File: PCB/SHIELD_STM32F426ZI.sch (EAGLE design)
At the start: 13 parts, among them IC1 AS4C16M16SA-6TCN, J1 104239-1430

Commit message: neuste vision
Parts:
- added R1, R2: 4.7k, sicom_universal:R_0402WEB_0402
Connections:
- removed net N$103: STM32F4G$5.PE1
- removed net N$111: STM32F4G$5.PG11
- removed net N$160: STM32F4G$6.PE0
- removed net N$23: STM32F4G$5.PC10
- removed net N$25: STM32F4G$5.PC12
- removed net N$54: STM32F4G$5.PD2
- new net N$1: STM32F4G$6.PB8
- net 3.3V: now also R1.2, R2.2
- net DCMI_D2: now also STM32F4G$6.PE0; no longer STM32F4G$6.PC8
- net DCMI_D3: now also STM32F4G$5.PE1; no longer STM32F4G$6.PC9
- net I2C1_SCL: now also R2.1
- net I2C1_SDA: now also R1.1
- net SDIO_CK: now also STM32F4G$5.PC12
- net SDIO_CMD: now also STM32F4G$5.PD2
- net SDIO_D0: now also STM32F4G$6.PC8
- net SDIO_D1: now also STM32F4G$6.PC9
- net SDIO_D2: now also STM32F4G$5.PC10
- net SDIO_D3: now also STM32F4G$5.PC11
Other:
- note added: "I2C"
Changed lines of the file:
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@@
 <part name="R30" library="rcl" library_urn="urn:adsk.eagle:library:334" deviceset="R-EU_" device="R0402" package3d_urn="urn:adsk.eagle:package:23547/3" value="100k"/>
 <part name="R31" library="rcl" library_urn="urn:adsk.eagle:library:334" deviceset="R-EU_" device="R0402" package3d_urn="urn:adsk.eagle:package:23547/3" value="100k"/>
+<part name="R1" library="sicom_universal" library_urn="urn:adsk.eagle:library:5101580" deviceset="R_0402" device="WEB_0402" package3d_urn="urn:adsk.eagle:package:23679/2" value="4.7k"/>
+<part name="R2" library="sicom_universal" library_urn="urn:adsk.eagle:library:5101580" deviceset="R_0402" device="WEB_0402" package3d_urn="urn:adsk.eagle:package:23679/2" value="4.7k"/>
 </parts>
 <sheets>
@@
 <pinref part="STM32F4" gate="G$5" pin="PG15"/>
 <wire x1="236.22" y1="66.04" x2="223.52" y2="66.04" width="0.1524" layer="91"/>
-<label x="213.36" y="66.04" size="1.778" layer="95"/>
+<label x="210.82" y="66.04" size="1.778" layer="95"/>
 </segment>
 </net>
@@
 <pinref part="STM32F4" gate="G$6" pin="PF11"/>
 <wire x1="43.18" y1="60.96" x2="30.48" y2="60.96" width="0.1524" layer="91"/>
-<label x="22.86" y="60.96" size="1.778" layer="95"/>
+<label x="20.32" y="60.96" size="1.778" layer="95"/>
 </segment>
 </net>
@@
 <pinref part="STM32F4" gate="G$6" pin="PG8"/>
 <wire x1="43.18" y1="55.88" x2="30.48" y2="55.88" width="0.1524" layer="91"/>
-<label x="22.86" y="55.88" size="1.778" layer="95"/>
+<label x="20.32" y="55.88" size="1.778" layer="95"/>
 </segment>
 </net>
@@
 </segment>
 </net>
-<net name="N$23" class="0">
+<net name="SDIO_D2" class="0">
 <segment>
 <pinref part="STM32F4" gate="G$5" pin="PC10"/>
 <wire x1="266.7" y1="144.78" x2="279.4" y2="144.78" width="0.1524" layer="91"/>
-</segment>
-</net>
-<net name="N$25" class="0">
+<label x="271.78" y="144.78" size="1.778" layer="95"/>
+</segment>
+</net>
+<net name="SDIO_CK" class="0">
 <segment>
 <pinref part="STM32F4" gate="G$5" pin="PC12"/>
 <wire x1="266.7" y1="142.24" x2="279.4" y2="142.24" width="0.1524" layer="91"/>
-</segment>
-</net>
-<net name="N$54" class="0">
+<label x="271.78" y="142.24" size="1.778" layer="95"/>
+</segment>
+</net>
+<net name="SDIO_CMD" class="0">
 <segment>
 <pinref part="STM32F4" gate="G$5" pin="PD2"/>
 <wire x1="236.22" y1="142.24" x2="223.52" y2="142.24" width="0.1524" layer="91"/>
+<label x="218.44" y="142.24" size="1.778" layer="95"/>
 </segment>
 </net>
@@
 </segment>
 </net>
-<net name="N$103" class="0">
-<segment>
-<pinref part="STM32F4" gate="G$5" pin="PE1"/>
-<wire x1="266.7" y1="68.58" x2="279.4" y2="68.58" width="0.1524" layer="91"/>
-</segment>
-</net>
 <net name="N$107" class="0">
 <segment>
@@
 </segment>
 </net>
-<net name="N$108" class="0">
-<segment>
-<pinref part="STM32F4" gate="G$5" pin="PG10"/>
-<wire x1="236.22" y1="63.5" x2="223.52" y2="63.5" width="0.1524" layer="91"/>
-</segment>
-</net>
 <net name="N$109" class="0">
 <segment>
@@
 </segment>
 </net>
-<net name="N$111" class="0">
-<segment>
-<pinref part="STM32F4" gate="G$5" pin="PG11"/>
-<wire x1="236.22" y1="58.42" x2="223.52" y2="58.42" width="0.1524" layer="91"/>
-</segment>
-</net>
 <net name="N$48" class="0">
 <segment>
@@
 <pinref part="STM32F4" gate="G$6" pin="PG14"/>
 <wire x1="73.66" y1="60.96" x2="86.36" y2="60.96" width="0.1524" layer="91"/>
-</segment>
-</net>
-<net name="N$160" class="0">
-<segment>
-<pinref part="STM32F4" gate="G$6" pin="PE0"/>
-<wire x1="43.18" y1="58.42" x2="30.48" y2="58.42" width="0.1524" layer="91"/>
 </segment>
 </net>
@@
 <pinref part="STM32F4" gate="G$5" pin="PE5"/>
 <wire x1="236.22" y1="83.82" x2="223.52" y2="83.82" width="0.1524" layer="91"/>
-<label x="218.44" y="83.82" size="1.9304" layer="95"/>
+<label x="215.9" y="83.82" size="1.9304" layer="95"/>
 </segment>
 </net>
@@
 </segment>
 <segment>
-<pinref part="STM32F4" gate="G$6" pin="PC9"/>
-<wire x1="73.66" y1="137.16" x2="86.36" y2="137.16" width="0.1524" layer="91"/>
-<label x="81.28" y="137.16" size="1.9304" layer="95"/>
+<pinref part="STM32F4" gate="G$5" pin="PE1"/>
+<wire x1="266.7" y1="68.58" x2="279.4" y2="68.58" width="0.1524" layer="91"/>
+<label x="274.32" y="68.58" size="1.778" layer="95"/>
 </segment>
 </net>
@@
 </segment>
 <segment>
-<pinref part="STM32F4" gate="G$6" pin="PC8"/>
-<wire x1="43.18" y1="137.16" x2="30.48" y2="137.16" width="0.1524" layer="91"/>
-<label x="25.4" y="137.16" size="1.9304" layer="95"/>
+<pinref part="STM32F4" gate="G$6" pin="PE0"/>
+<wire x1="43.18" y1="58.42" x2="30.48" y2="58.42" width="0.1524" layer="91"/>
+<label x="25.4" y="58.42" size="1.778" layer="95"/>
 </segment>
 </net>
@@
 <wire x1="-15.24" y1="15.24" x2="0" y2="15.24" width="0.1524" layer="91"/>
 <label x="-7.62" y="15.24" size="1.9304" layer="95"/>
+</segment>
+</net>
+<net name="N$1" class="0">
+<segment>
+<pinref part="STM32F4" gate="G$6" pin="PB8"/>
+<wire x1="73.66" y1="134.62" x2="86.36" y2="134.62" width="0.1524" layer="91"/>
+</segment>
+</net>
+<net name="SDIO_D1" class="0">
+<segment>
+<pinref part="STM32F4" gate="G$6" pin="PC9"/>
+<wire x1="73.66" y1="137.16" x2="86.36" y2="137.16" width="0.1524" layer="91"/>
+<label x="78.74" y="137.16" size="1.778" layer="95"/>
+</segment>
+</net>
+<net name="SDIO_D0" class="0">
+<segment>
+<pinref part="STM32F4" gate="G$6" pin="PC8"/>
+<wire x1="43.18" y1="137.16" x2="30.48" y2="137.16" width="0.1524" layer="91"/>
+<label x="27.94" y="137.16" size="1.778" layer="95"/>
+</segment>
+</net>
+<net name="SDIO_D3" class="0">
+<segment>
+<pinref part="STM32F4" gate="G$5" pin="PC11"/>
+<wire x1="236.22" y1="144.78" x2="223.52" y2="144.78" width="0.1524" layer="91"/>
+<label x="220.98" y="144.78" size="1.778" layer="95"/>
+</segment>
+</net>
+<net name="N$2" class="0">
+<segment>
+<pinref part="STM32F4" gate="G$5" pin="PG10"/>
+<wire x1="236.22" y1="63.5" x2="223.52" y2="63.5" width="0.1524" layer="91"/>
 </segment>
 </net>
@@
 <plain>
 <text x="66.04" y="88.9" size="3.81" layer="91">SDCARD_MODUL</text>
+<text x="205.232" y="95.758" size="3.81" layer="90">I2C</text>
 </plain>
 <instances>
@@
 <attribute name="NAME" x="138.6586" y="107.95" size="1.778" layer="95" rot="R270"/>
 <attribute name="VALUE" x="133.858" y="107.95" size="1.778" layer="96" rot="R270"/>
+</instance>
+<instance part="R1" gate="G$1" x="223.012" y="72.898" smashed="yes" rot="R90">
+<attribute name="NAME" x="221.5134" y="69.088" size="1.778" layer="95" rot="R90"/>
+<attribute name="VALUE" x="226.314" y="69.088" size="1.778" layer="96" rot="R90"/>
+</instance>
+<instance part="R2" gate="G$1" x="230.632" y="72.898" smashed="yes" rot="R90">
+<attribute name="NAME" x="229.1334" y="69.088" size="1.778" layer="95" rot="R90"/>
+<attribute name="VALUE" x="233.934" y="69.088" size="1.778" layer="96" rot="R90"/>
 </instance>
 </instances>
@@
 <label x="132.08" y="132.08" size="1.778" layer="95"/>
 </segment>
-</net>
+<segment>
+<wire x1="223.012" y1="77.978" x2="223.012" y2="83.058" width="0.1524" layer="91"/>
+<wire x1="223.012" y1="83.058" x2="223.012" y2="93.218" width="0.1524" layer="91"/>
+<wire x1="230.632" y1="77.978" x2="230.632" y2="83.058" width="0.1524" layer="91"/>
+<wire x1="230.632" y1="83.058" x2="223.012" y2="83.058" width="0.1524" layer="91"/>
+<junction x="223.012" y="83.058"/>
+<wire x1="223.012" y1="93.218" x2="210.312" y2="93.218" width="0.1524" layer="91"/>
+<pinref part="R1" gate="G$1" pin="2"/>
+<pinref part="R2" gate="G$1" pin="2"/>
+<label x="212.852" y="93.218" size="1.778" layer="95"/>
+</segment>
+</net>
+<net name="I2C1_SDA" class="0">
+<segment>
+<wire x1="210.312" y1="60.198" x2="223.012" y2="60.198" width="0.1524" layer="91"/>
+<wire x1="223.012" y1="60.198" x2="245.872" y2="60.198" width="0.1524" layer="91"/>
+<wire x1="223.012" y1="60.198" x2="223.012" y2="67.818" width="0.1524" layer="91"/>
+<junction x="223.012" y="60.198"/>
+<pinref part="R1" gate="G$1" pin="1"/>
+<label x="207.772" y="60.198" size="1.778" layer="95"/>
+</segment>
+</net>
+<net name="I2C1_SCL" class="0">
+<segment>
+<wire x1="210.312" y1="57.658" x2="230.632" y2="57.658" width="0.1524" layer="91"/>
+<wire x1="230.632" y1="57.658" x2="245.872" y2="57.658" width="0.1524" layer="91"/>
+<wire x1="230.632" y1="57.658" x2="230.632" y2="67.818" width="0.1524" layer="91"/>
+<pinref part="R2" gate="G$1" pin="1"/>
+<label x="207.772" y="57.658" size="1.778" layer="95"/>
+<junction x="230.632" y="57.658"/>
+</segment>
+</net>

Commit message: neuster Stand
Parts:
- added R3: 10k, sicom_universal:R_0402WEB_0402
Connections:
- net N$1 renamed A
- removed net N$19: IC1.CS#
- net 3.3V: now also R3.2
- net FMC_SDNE0: now also IC1.CS#, R3.1
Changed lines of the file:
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@@
 <part name="R1" library="sicom_universal" library_urn="urn:adsk.eagle:library:5101580" deviceset="R_0402" device="WEB_0402" package3d_urn="urn:adsk.eagle:package:23679/2" value="4.7k"/>
 <part name="R2" library="sicom_universal" library_urn="urn:adsk.eagle:library:5101580" deviceset="R_0402" device="WEB_0402" package3d_urn="urn:adsk.eagle:package:23679/2" value="4.7k"/>
+<part name="R3" library="sicom_universal" library_urn="urn:adsk.eagle:library:5101580" deviceset="R_0402" device="WEB_0402" package3d_urn="urn:adsk.eagle:package:23679/2" value="10k"/>
 </parts>
 <sheets>
@@
 <attribute name="VALUE" x="-85.725" y="98.425" size="1.778" layer="96"/>
 </instance>
+<instance part="R3" gate="G$1" x="-63.5" y="83.82" smashed="yes" rot="R90">
+<attribute name="NAME" x="-64.9986" y="80.01" size="1.778" layer="95" rot="R90"/>
+<attribute name="VALUE" x="-60.198" y="80.01" size="1.778" layer="96" rot="R90"/>
+</instance>
 </instances>
 <busses>
@@
 <wire x1="43.18" y1="60.96" x2="30.48" y2="60.96" width="0.1524" layer="91"/>
 <label x="20.32" y="60.96" size="1.778" layer="95"/>
-</segment>
-</net>
-<net name="N$19" class="0">
-<segment>
-<pinref part="IC1" gate="G$1" pin="CS#"/>
-<wire x1="-33.02" y1="76.2" x2="-45.72" y2="76.2" width="0.1524" layer="91"/>
 </segment>
 </net>
@@
 <label x="-43.18" y="55.88" size="1.9304" layer="95"/>
 </segment>
+<segment>
+<pinref part="R3" gate="G$1" pin="2"/>
+<wire x1="-63.5" y1="88.9" x2="-63.5" y2="93.98" width="0.1524" layer="91"/>
+<label x="-63.5" y="93.98" size="1.778" layer="95"/>
+</segment>
 </net>
 <net name="N$65" class="0">
@@
 <label x="274.32" y="101.6" size="1.778" layer="95"/>
 </segment>
+<segment>
+<pinref part="IC1" gate="G$1" pin="CS#"/>
+<pinref part="R3" gate="G$1" pin="1"/>
+<wire x1="-63.5" y1="78.74" x2="-63.5" y2="76.2" width="0.1524" layer="91"/>
+<wire x1="-63.5" y1="76.2" x2="-33.02" y2="76.2" width="0.1524" layer="91"/>
+<wire x1="-78.74" y1="76.2" x2="-63.5" y2="76.2" width="0.1524" layer="91"/>
+<junction x="-63.5" y="76.2"/>
+<label x="-78.74" y="76.2" size="1.778" layer="95"/>
+</segment>
 </net>
 <net name="N$81" class="0">
@@
 </segment>
 </net>
-<net name="N$1" class="0">
-<segment>
-<pinref part="STM32F4" gate="G$6" pin="PB8"/>
-<wire x1="73.66" y1="134.62" x2="86.36" y2="134.62" width="0.1524" layer="91"/>
-</segment>
-</net>
 <net name="SDIO_D1" class="0">
 <segment>
@@
 </segment>
 </net>
+<net name="A" class="0">
+<segment>
+<pinref part="STM32F4" gate="G$6" pin="PB8"/>
+<wire x1="73.66" y1="134.62" x2="86.36" y2="134.62" width="0.1524" layer="91"/>
+</segment>
+</net>

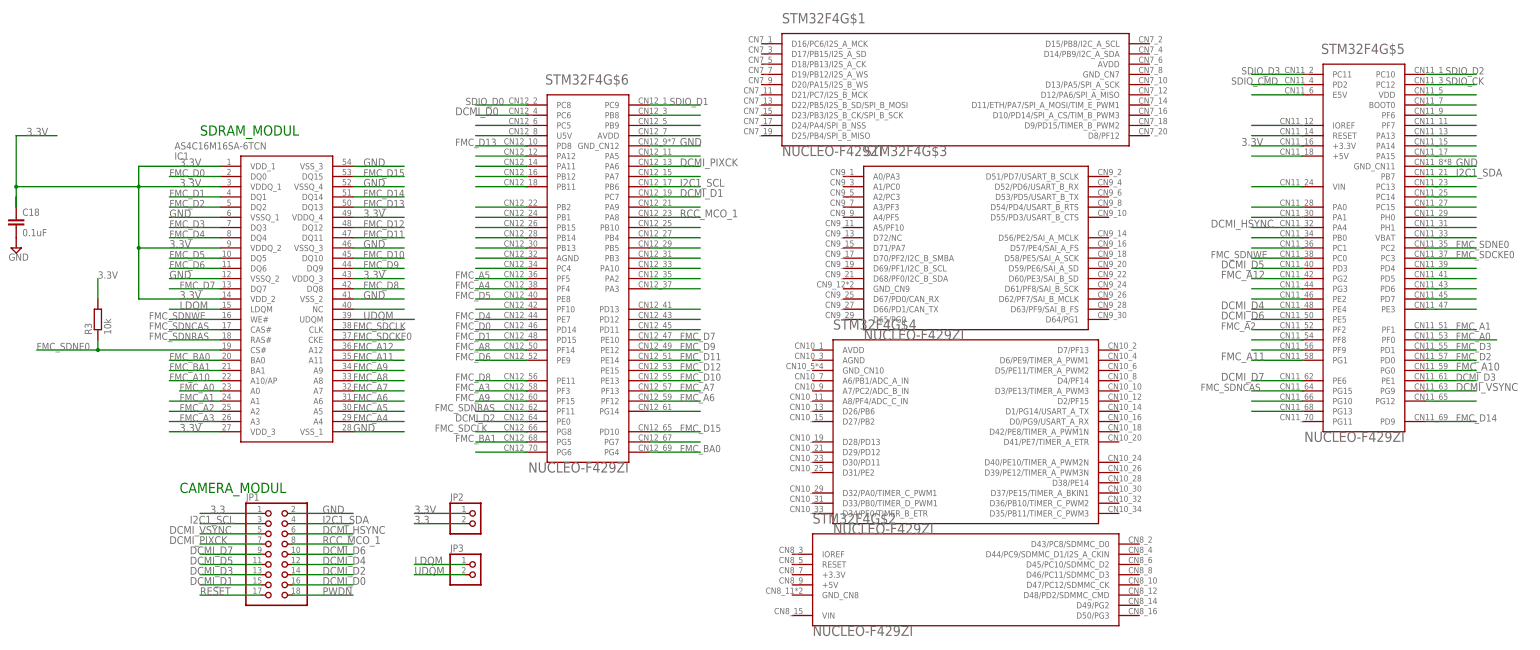
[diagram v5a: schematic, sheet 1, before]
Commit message: modyfi fault by ERC and DRC
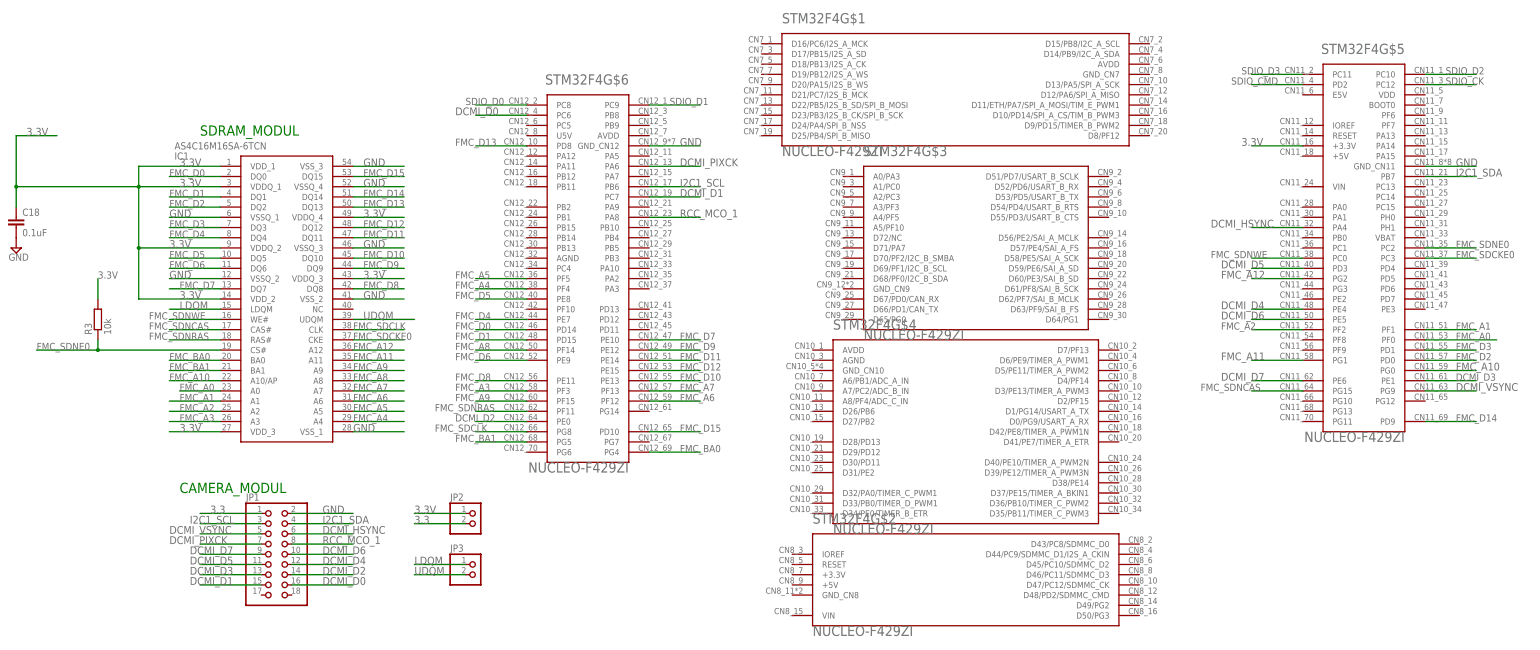
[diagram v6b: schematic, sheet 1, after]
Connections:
- removed net 3V3: J1.T4_VDD
- removed net A: STM32F4G$6.PB8
- removed net N$107: STM32F4G$5.PG12
- removed net N$109: STM32F4G$5.PG13
- removed net N$112: STM32F4G$6.PA12
- removed net N$114: STM32F4G$6.PA11
- removed net N$115: STM32F4G$6.PA7
- removed net N$116: STM32F4G$6.PB12
- removed net N$118: STM32F4G$6.PB11
- removed net N$120: STM32F4G$6.PA9
- removed net N$121: STM32F4G$6.PB2
- removed net N$123: STM32F4G$6.PB1
- removed net N$124: STM32F4G$6.PB10
- removed net N$125: STM32F4G$6.PB15
- removed net N$126: STM32F4G$6.PB4
- removed net N$127: STM32F4G$6.PB14
- removed net N$128: STM32F4G$6.PB5
- removed net N$129: STM32F4G$6.PB13
- removed net N$130: STM32F4G$6.PB3
- removed net N$131: STM32F4G$6.AGND
- removed net N$132: STM32F4G$6.PA10
- removed net N$133: STM32F4G$6.PC4
- removed net N$134: STM32F4G$6.PA2
- removed net N$136: STM32F4G$6.PA3
- removed net N$139: STM32F4G$6.PD13
- removed net N$140: STM32F4G$6.PF10
- removed net N$141: STM32F4G$6.PD12
- removed net N$143: STM32F4G$6.PD11
- removed net N$158: STM32F4G$6.PG14
- removed net N$163: STM32F4G$6.PG7
- removed net N$166: STM32F4G$6.PG6
- removed net N$2: STM32F4G$5.PG10
- removed net N$41: IC1.NC
- removed net N$48: STM32F4G$6.PB9
- removed net N$49: STM32F4G$6.PC5
- removed net N$50: STM32F4G$6.AVDD
- removed net N$51: STM32F4G$6.U5V
- removed net N$55: STM32F4G$5.VDD
- removed net N$56: STM32F4G$5.E5V
- removed net N$57: STM32F4G$5.BOOT0
- removed net N$58: STM32F4G$5.PF6
- removed net N$59: STM32F4G$5.PF7
- removed net N$60: STM32F4G$5.IOREF
- removed net N$61: STM32F4G$5.PA13
- removed net N$62: STM32F4G$5.RESET
- removed net N$63: STM32F4G$5.PA14
- removed net N$65: STM32F4G$5.PA15
- removed net N$66: STM32F4G$5.+5V
- removed net N$69: STM32F4G$5.PC13
- removed net N$70: STM32F4G$5.VIN
- removed net N$71: STM32F4G$5.PC14
- removed net N$72: STM32F4G$5.PC15
- removed net N$73: STM32F4G$5.PA0
- removed net N$74: STM32F4G$5.PH0
- removed net N$75: STM32F4G$5.PA1
- removed net N$76: STM32F4G$5.PH1
- removed net N$78: STM32F4G$5.VBAT
- removed net N$79: STM32F4G$5.PB0
- removed net N$81: STM32F4G$5.PC1
- removed net N$84: STM32F4G$5.PD4
- removed net N$86: STM32F4G$5.PD5
- removed net N$88: STM32F4G$5.PD6
- removed net N$89: STM32F4G$5.PG3
- removed net N$90: STM32F4G$5.PD7
- removed net N$91: STM32F4G$5.PE2
- removed net N$92: STM32F4G$5.PE3
- removed net N$96: STM32F4G$6.PA5
- removed net N$97: STM32F4G$5.PF8
- removed net N$99: STM32F4G$5.PF9
- removed net PWDN: JP1.18
- removed net RESET: JP1.17
- net 3.3V: now also J1.T4_VDD

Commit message: PCB wurde mit kurzer Leitung korrigiert
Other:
- moved on the sheet: C18, IC1, R3, STM32F4G$5, STM32F4G$6

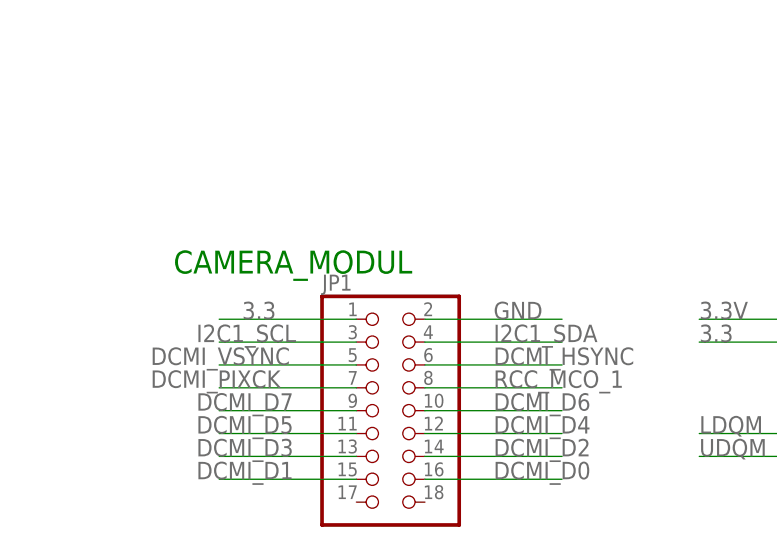
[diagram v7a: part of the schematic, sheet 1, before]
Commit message: Namen der Elementen und Pin hinzufügen
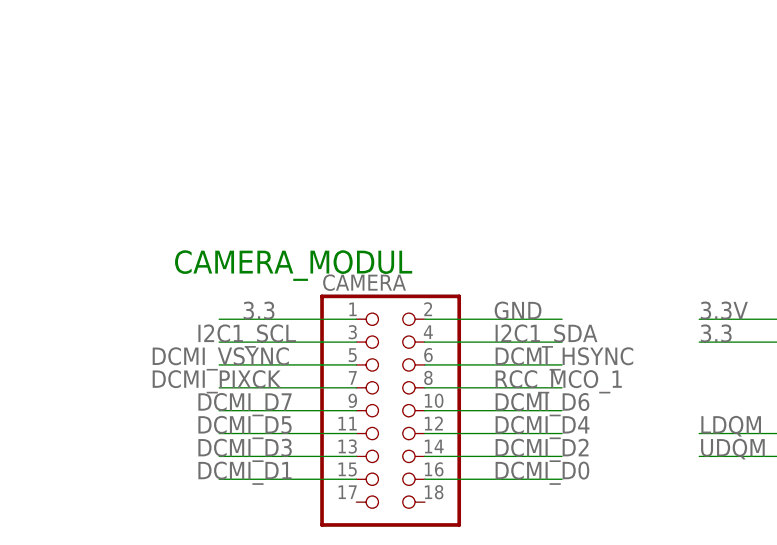
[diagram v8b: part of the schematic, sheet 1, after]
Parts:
- renumbered J1 to SDCARD, JP1 to CAMERA
